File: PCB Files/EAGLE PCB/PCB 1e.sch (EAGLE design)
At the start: 30 parts

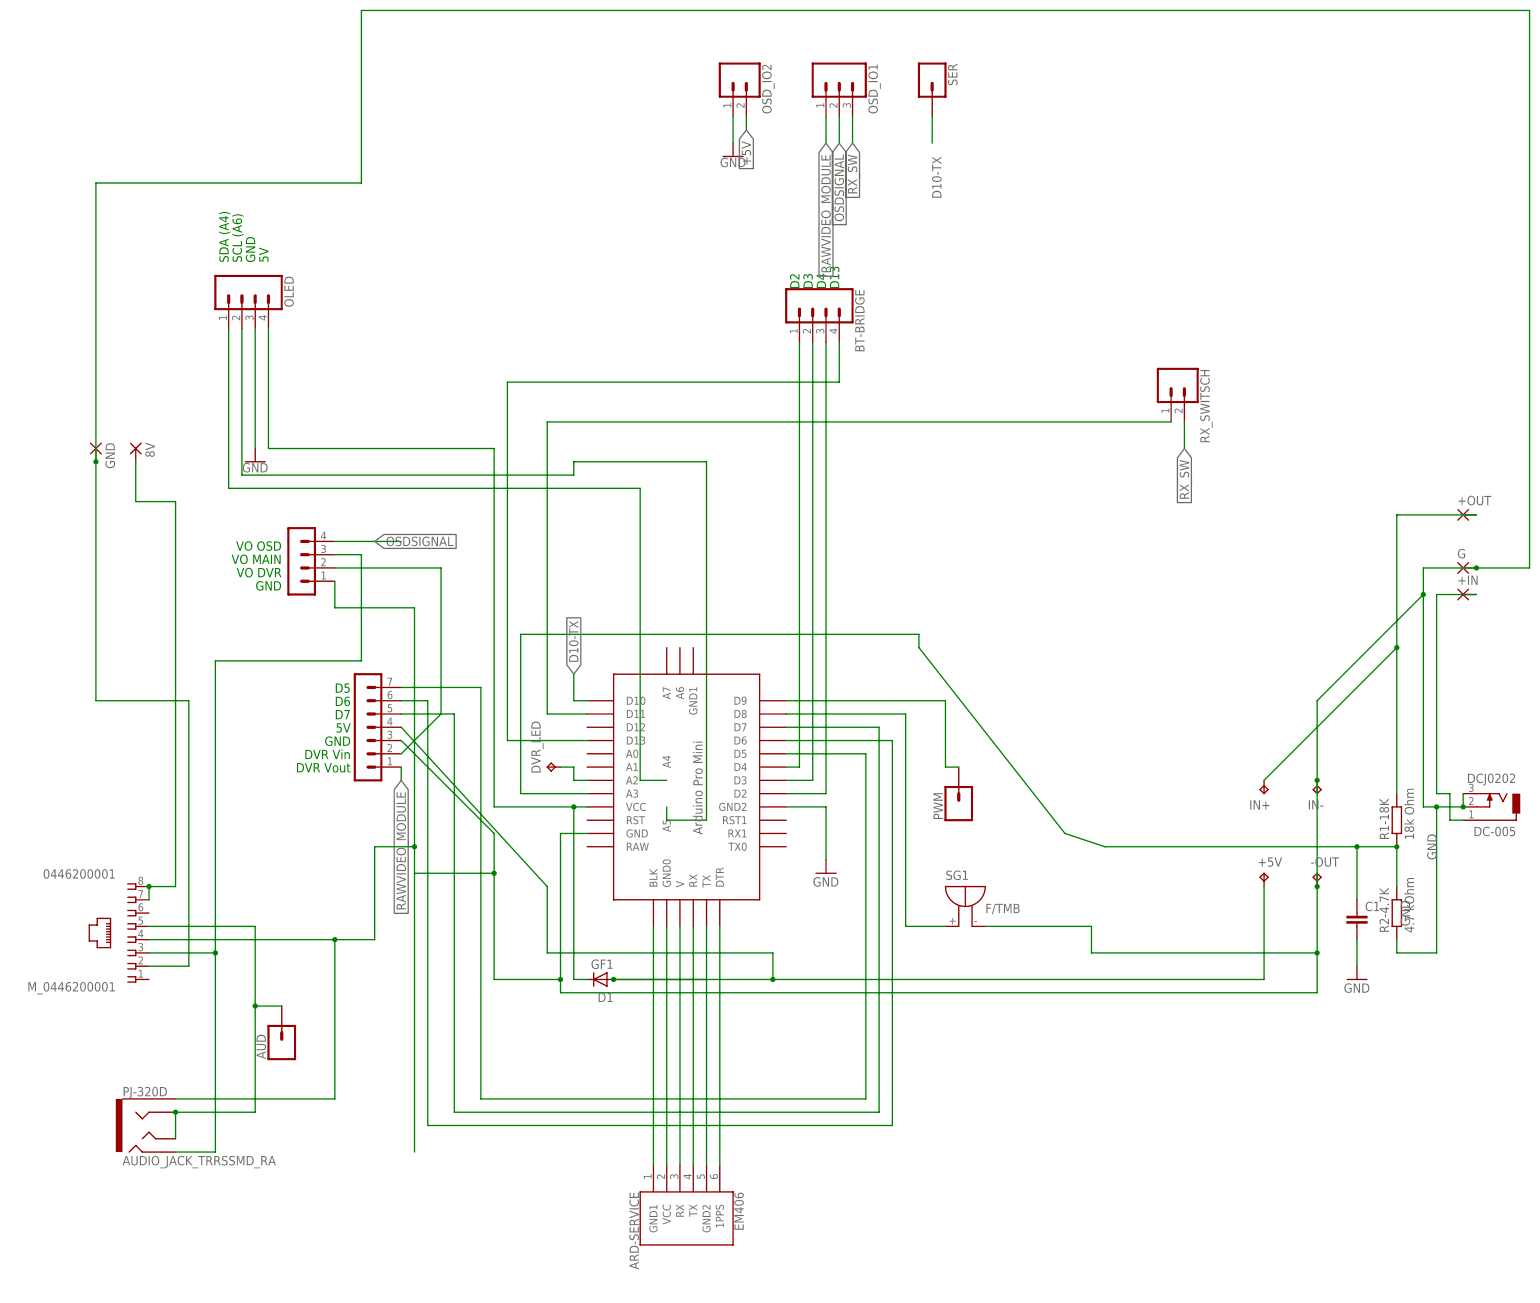
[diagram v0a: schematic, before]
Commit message: new pcb1 revision 3 (5v on RJ45 and OSD PCB footprint added)
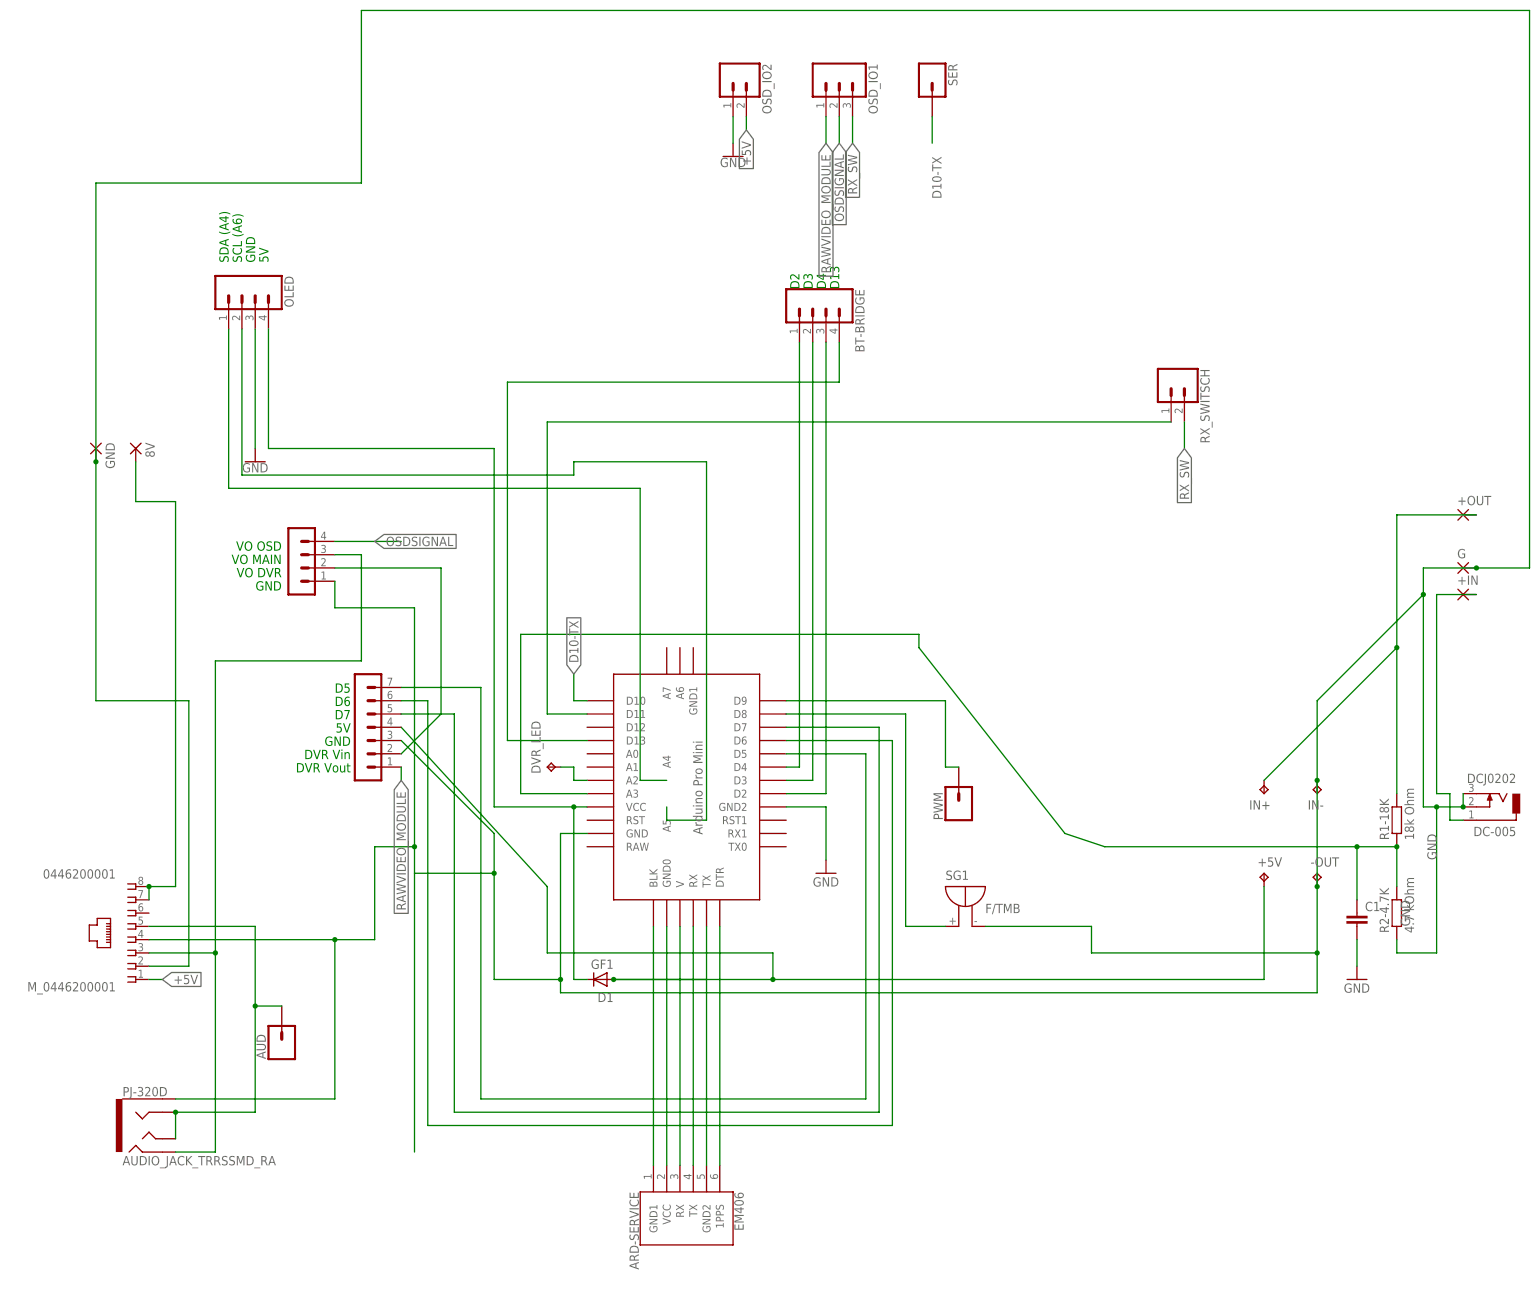
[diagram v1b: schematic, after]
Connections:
- net +5V: now also M_0446200001.1

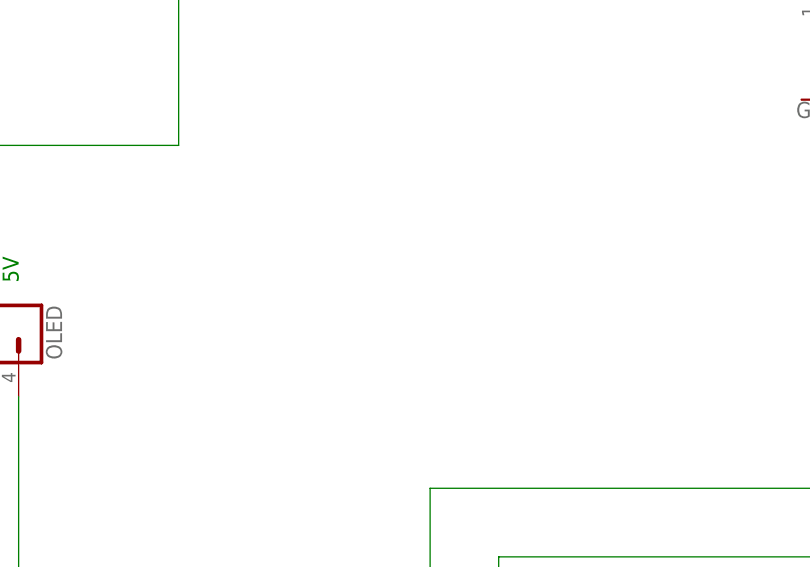
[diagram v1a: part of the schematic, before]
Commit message: added 75ohm resistor to pcb
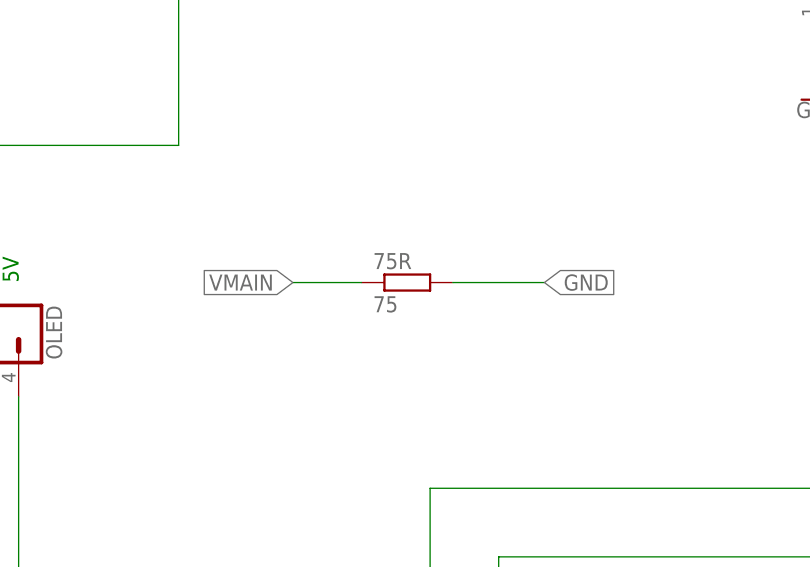
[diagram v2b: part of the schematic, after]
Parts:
- added 75R: 75, resistor:R-EU_R0603
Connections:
- net GND: now also 75R.2
- net VMAIN: now also 75R.1
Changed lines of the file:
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@@
 <grid distance="0.1" unitdist="inch" unit="inch" style="lines" multiple="1" display="no" altdistance="0.01" altunitdist="inch" altunit="inch"/>
 <layers>
-<layer number="1" name="Top" color="4" fill="1" visible="no" active="no"/>
-<layer number="2" name="Route2" color="1" fill="3" visible="no" active="no"/>
-<layer number="3" name="Route3" color="4" fill="3" visible="no" active="no"/>
-<layer number="4" name="Route4" color="1" fill="4" visible="no" active="no"/>
-<layer number="5" name="Route5" color="4" fill="4" visible="no" active="no"/>
-<layer number="6" name="Route6" color="1" fill="8" visible="no" active="no"/>
-<layer number="7" name="Route7" color="4" fill="8" visible="no" active="no"/>
-<layer number="8" name="Route8" color="1" fill="2" visible="no" active="no"/>
-<layer number="9" name="Route9" color="4" fill="2" visible="no" active="no"/>
-<layer number="10" name="Route10" color="1" fill="7" visible="no" active="no"/>
-<layer number="11" name="Route11" color="4" fill="7" visible="no" active="no"/>
-<layer number="12" name="Route12" color="1" fill="5" visible="no" active="no"/>
-<layer number="13" name="Route13" color="4" fill="5" visible="no" active="no"/>
-<layer number="14" name="Route14" color="1" fill="6" visible="no" active="no"/>
-<layer number="15" name="Route15" color="4" fill="6" visible="no" active="no"/>
-<layer number="16" name="Bottom" color="1" fill="1" visible="no" active="no"/>
-<layer number="17" name="Pads" color="2" fill="1" visible="no" active="no"/>
-<layer number="18" name="Vias" color="2" fill="1" visible="no" active="no"/>
-<layer number="19" name="Unrouted" color="6" fill="1" visible="no" active="no"/>
-<layer number="20" name="Dimension" color="24" fill="1" visible="no" active="no"/>
-<layer number="21" name="tPlace" color="7" fill="1" visible="no" active="no"/>
-<layer number="22" name="bPlace" color="7" fill="1" visible="no" active="no"/>
-<layer number="23" name="tOrigins" color="15" fill="1" visible="no" active="no"/>
-<layer number="24" name="bOrigins" color="15" fill="1" visible="no" active="no"/>
-<layer number="25" name="tNames" color="7" fill="1" visible="no" active="no"/>
-<layer number="26" name="bNames" color="7" fill="1" visible="no" active="no"/>
-<layer number="27" name="tValues" color="7" fill="1" visible="no" active="no"/>
-<layer number="28" name="bValues" color="7" fill="1" visible="no" active="no"/>
+<layer number="1" name="Top" color="4" fill="1" visible="yes" active="no"/>
+<layer number="2" name="Route2" color="1" fill="3" visible="yes" active="no"/>
+<layer number="3" name="Route3" color="4" fill="3" visible="yes" active="no"/>
+<layer number="4" name="Route4" color="1" fill="4" visible="yes" active="no"/>
+<layer number="5" name="Route5" color="4" fill="4" visible="yes" active="no"/>
+<layer number="6" name="Route6" color="1" fill="8" visible="yes" active="no"/>
+<layer number="7" name="Route7" color="4" fill="8" visible="yes" active="no"/>
+<layer number="8" name="Route8" color="1" fill="2" visible="yes" active="no"/>
+<layer number="9" name="Route9" color="4" fill="2" visible="yes" active="no"/>
+<layer number="10" name="Route10" color="1" fill="7" visible="yes" active="no"/>
+<layer number="11" name="Route11" color="4" fill="7" visible="yes" active="no"/>
+<layer number="12" name="Route12" color="1" fill="5" visible="yes" active="no"/>
+<layer number="13" name="Route13" color="4" fill="5" visible="yes" active="no"/>
+<layer number="14" name="Route14" color="1" fill="6" visible="yes" active="no"/>
+<layer number="15" name="Route15" color="4" fill="6" visible="yes" active="no"/>
+<layer number="16" name="Bottom" color="1" fill="1" visible="yes" active="no"/>
+<layer number="17" name="Pads" color="2" fill="1" visible="yes" active="no"/>
+<layer number="18" name="Vias" color="2" fill="1" visible="yes" active="no"/>
+<layer number="19" name="Unrouted" color="6" fill="1" visible="yes" active="no"/>
+<layer number="20" name="Dimension" color="24" fill="1" visible="yes" active="no"/>
+<layer number="21" name="tPlace" color="7" fill="1" visible="yes" active="no"/>
+<layer number="22" name="bPlace" color="7" fill="1" visible="yes" active="no"/>
+<layer number="23" name="tOrigins" color="15" fill="1" visible="yes" active="no"/>
+<layer number="24" name="bOrigins" color="15" fill="1" visible="yes" active="no"/>
+<layer number="25" name="tNames" color="7" fill="1" visible="yes" active="no"/>
+<layer number="26" name="bNames" color="7" fill="1" visible="yes" active="no"/>
+<layer number="27" name="tValues" color="7" fill="1" visible="yes" active="no"/>
+<layer number="28" name="bValues" color="7" fill="1" visible="yes" active="no"/>
 <layer number="29" name="tStop" color="7" fill="3" visible="no" active="no"/>
 <layer number="30" name="bStop" color="7" fill="6" visible="no" active="no"/>
@@
 <layer number="35" name="tGlue" color="7" fill="4" visible="no" active="no"/>
 <layer number="36" name="bGlue" color="7" fill="5" visible="no" active="no"/>
-<layer number="37" name="tTest" color="7" fill="1" visible="no" active="no"/>
-<layer number="38" name="bTest" color="7" fill="1" visible="no" active="no"/>
+<layer number="37" name="tTest" color="7" fill="1" visible="yes" active="no"/>
+<layer number="38" name="bTest" color="7" fill="1" visible="yes" active="no"/>
 <layer number="39" name="tKeepout" color="4" fill="11" visible="no" active="no"/>
 <layer number="40" name="bKeepout" color="1" fill="11" visible="no" active="no"/>
@@
 <layer number="44" name="Drills" color="7" fill="1" visible="no" active="no"/>
 <layer number="45" name="Holes" color="7" fill="1" visible="no" active="no"/>
-<layer number="46" name="Milling" color="3" fill="1" visible="no" active="no"/>
-<layer number="47" name="Measures" color="7" fill="1" visible="no" active="no"/>
-<layer number="48" name="Document" color="7" fill="1" visible="no" active="no"/>
-<layer number="49" name="Reference" color="7" fill="1" visible="no" active="no"/>
-<layer number="50" name="dxf" color="7" fill="1" visible="no" active="no"/>
-<layer number="51" name="tDocu" color="7" fill="1" visible="no" active="no"/>
-<layer number="52" name="bDocu" color="7" fill="1" visible="no" active="no"/>
-<layer number="53" name="tGND_GNDA" color="7" fill="9" visible="no" active="no"/>
-<layer number="54" name="bGND_GNDA" color="1" fill="9" visible="no" active="no"/>
-<layer number="56" name="wert" color="7" fill="1" visible="no" active="no"/>
-<layer number="57" name="tCAD" color="7" fill="1" visible="no" active="no"/>
-<layer number="59" name="tCarbon" color="7" fill="1" visible="no" active="no"/>
-<layer number="60" name="bCarbon" color="7" fill="1" visible="no" active="no"/>
+<layer number="46" name="Milling" color="3" fill="1" visible="yes" active="no"/>
+<layer number="47" name="Measures" color="7" fill="1" visible="yes" active="no"/>
+<layer number="48" name="Document" color="7" fill="1" visible="yes" active="no"/>
+<layer number="49" name="Reference" color="7" fill="1" visible="yes" active="no"/>
+<layer number="50" name="dxf" color="7" fill="1" visible="yes" active="no"/>
+<layer number="51" name="tDocu" color="7" fill="1" visible="yes" active="no"/>
+<layer number="52" name="bDocu" color="7" fill="1" visible="yes" active="no"/>
+<layer number="53" name="tGND_GNDA" color="7" fill="9" visible="yes" active="no"/>
+<layer number="54" name="bGND_GNDA" color="1" fill="9" visible="yes" active="no"/>
+<layer number="56" name="wert" color="7" fill="1" visible="yes" active="no"/>
+<layer number="57" name="tCAD" color="7" fill="1" visible="yes" active="no"/>
+<layer number="59" name="tCarbon" color="7" fill="1" visible="yes" active="no"/>
+<layer number="60" name="bCarbon" color="7" fill="1" visible="yes" active="no"/>
 <layer number="88" name="SimResults" color="9" fill="1" visible="yes" active="yes"/>
 <layer number="89" name="SimProbes" color="9" fill="1" visible="yes" active="yes"/>
@@
 <part name="GND3" library="SparkFun-PowerSymbols" library_urn="urn:adsk.eagle:library:530" deviceset="GND" device=""/>
 <part name="GND4" library="SparkFun-PowerSymbols" library_urn="urn:adsk.eagle:library:530" deviceset="GND" device=""/>
+<part name="75R" library="resistor" library_urn="urn:adsk.eagle:library:348" deviceset="R-EU_" device="R0603" package3d_urn="urn:adsk.eagle:package:23555/2" value="75"/>
 </parts>
 <sheets>
@@
 <instance part="GND4" gate="1" x="99.06" y="162.56" smashed="yes">
 <attribute name="VALUE" x="99.06" y="162.306" size="1.778" layer="96" align="top-center"/>
+</instance>
+<instance part="75R" gate="G$1" x="144.78" y="200.66" smashed="yes">
+<attribute name="NAME" x="140.97" y="202.1586" size="1.778" layer="95"/>
+<attribute name="VALUE" x="140.97" y="197.358" size="1.778" layer="96"/>
 </instance>
 </instances>
@@
 <pinref part="GND4" gate="1" pin="GND"/>
 </segment>
+<segment>
+<pinref part="75R" gate="G$1" pin="2"/>
+<wire x1="149.86" y1="200.66" x2="160.02" y2="200.66" width="0.1524" layer="91"/>
+<label x="160.02" y="200.66" size="1.778" layer="95" xref="yes"/>
+</segment>
 </net>
 <net name="RAWVIDEO_MODULE" class="2">
@@
 <wire x1="91.44" y1="30.48" x2="83.82" y2="30.48" width="0.1524" layer="91"/>
 </segment>
-</net>
+<segment>
+<pinref part="75R" gate="G$1" pin="1"/>
+<wire x1="139.7" y1="200.66" x2="132.08" y2="200.66" width="0.1524" layer="91"/>
+<label x="132.08" y="200.66" size="1.778" layer="95" rot="R180" xref="yes"/>
+</segment>
+</net>
